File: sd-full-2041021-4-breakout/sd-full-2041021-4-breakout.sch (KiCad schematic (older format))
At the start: 0 parts

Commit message: Update docs. Release full SD breakout v1.0
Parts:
- added C1, C4: 1uF, Wickerlib:RLC-0603-SMD, symbol CAP-CER-1UF-25V-X7R-0603
- added C2, C3: 0.1uF, Wickerlib:RLC-0603-SMD, symbol CAP-CER-0.1UF-100V-X7R-0603
- added J1: BREAKOUT, Wickerlib:CONN-HEADER-STRAIGHT-P2.54MM-1x06, symbol HEADER-MALE-6POS-TH-1x06-P0.1IN
- added J2: TE CONN 2041021-4, Wickerlib:CONN-SD-FULL-TECONN-2041021-4, symbol CONN-SD-CARD-PUSH-PULL-R/A-SMD
- added U1: MIC5365 150mA, Wickerlib:SOT-353, symbol IC-REG-LDO-3.3V-0.15A-MIC5365-SOT353
- added U2: TXB0104, Wickerlib:SOIC-14-3.9x8.7MM-P1.27MM, symbol IC-VOLT-LEVEL-TRANSLATOR-TXB0104-SOIC14
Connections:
- new net +3V3: C3.1, C4.1, J2.4 (VCC), U1.5 (VOUT), U2.1 (VCCA), U2.8 (OE)
- new net CS: J1.5 (P5), U2.10 (B4)
- new net GND: C1.2, C2.2, C3.2, C4.2, J1.6 (P6), J2.13 (GND), J2.3 (VSS), J2.6 (VSS), U1.2 (GND), U2.7 (GND)
- new net MISO: J1.2 (P2), U2.13 (B1)
- new net MOSI: J1.4 (P4), U2.11 (B3)
- new net SCLK: J1.3 (P3), U2.12 (B2)
- new net SD_CS: J2.1 (CS), U2.5 (A4)
- new net SD_MISO: J2.7 (DATA_OUT), U2.2 (A1)
- new net SD_MOSI: J2.2 (DATA_IN), U2.4 (A3)
- new net SD_SCLK: J2.5 (SCLK), U2.3 (A2)
- new net VIN: C1.1, C2.1, J1.1 (P1), U1.1 (VIN), U1.3 (STBY), U2.14 (VCCB)

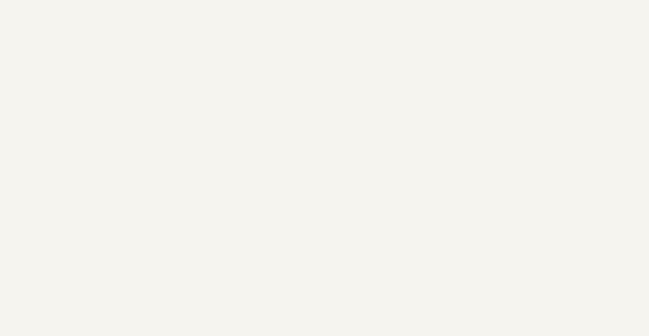
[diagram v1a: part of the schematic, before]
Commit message: Created schematic images. Updated README.
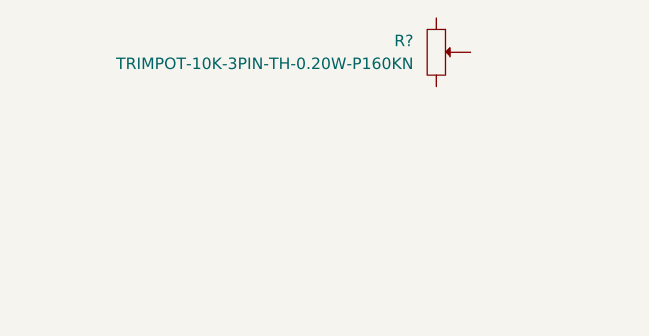
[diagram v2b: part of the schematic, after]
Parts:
- added R?: TRIMPOT-10K-3PIN-TH-0.20W-P160KN, Wickerlib:RES-TRIMPOT-TTELEC-P160-TH, symbol TRIMPOT-10K-3PIN-TH-0.20W-P160KN
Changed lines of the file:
@@
 EESchema Schematic File Version 2
 LIBS:wickerlib
+LIBS:crazy_circuits
+LIBS:sd-full-2041021-4-breakout-cache
 EELAYER 25 0
 EELAYER END
@@
 	7050 4800 6825 4800
 Connection ~ 6825 4800
+$Comp
+L TRIMPOT-10K-3PIN-TH-0.20W-P160KN R?
+U 1 1 5882C571
+P 2225 2025
+F 0 "R?" H 2125 2075 50  0000 R CNN
+F 1 "TRIMPOT-10K-3PIN-TH-0.20W-P160KN" H 2125 1975 50  0000 R CNN
+F 2 "Wickerlib:RES-TRIMPOT-TTELEC-P160-TH" H 2225 1675 50  0001 C CIN
+F 3 "http://www.bitechnologies.com/pdfs/p160.pdf" V 2225 2025 5   0001 C CNN
+F 4 "POT 10K OHM 1/5W PLASTIC LINEAR" H 2225 1675 50  0001 C CIN "Description"
+F 5 "TT Electronics" H 2225 1675 50  0001 C CIN "MF_Name"
+F 6 "P160KN-0QC15B10K" H 2225 1675 50  0001 C CIN "MF_PN"
+F 7 "Digikey" H 2225 1675 50  0001 C CIN "S1_Name"
+F 8 "987-1301-ND" H 2225 1675 50  0001 C CIN "S1_PN"
+	1    2225 2025
+	1    0    0    -1
+$EndComp
 $EndSCHEMATC
